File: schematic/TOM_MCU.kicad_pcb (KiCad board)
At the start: 4 copper layers, 236 parts, among them J1 22053041, J10 Conn_01x02, J11 Conn_01x02, J2 22053041, J3 USB4216-03-A, J4 USB4216-03-A, J5 E1E2-Emulator-Interface, J6 EMU CFG, J7 UPSEL_CFG, J8 Conn_01x02, J9 Conn_01x02, SW1 OP_CFG, U1 TVS2200DRV, U10 DS18B20+, U2 TVS2200DRV, U3 LDL1117S33R, U4 CY7C65213A-28PVXI, U5 TPS2116DRLR, U6 TXS0102DCUT, U7 TXS0102DCUT, U8 MIC5205-2.5YM5-TR, U9 R5F572NNHGFP-30, Y1 ECS-240-8-30B-CKM-TR

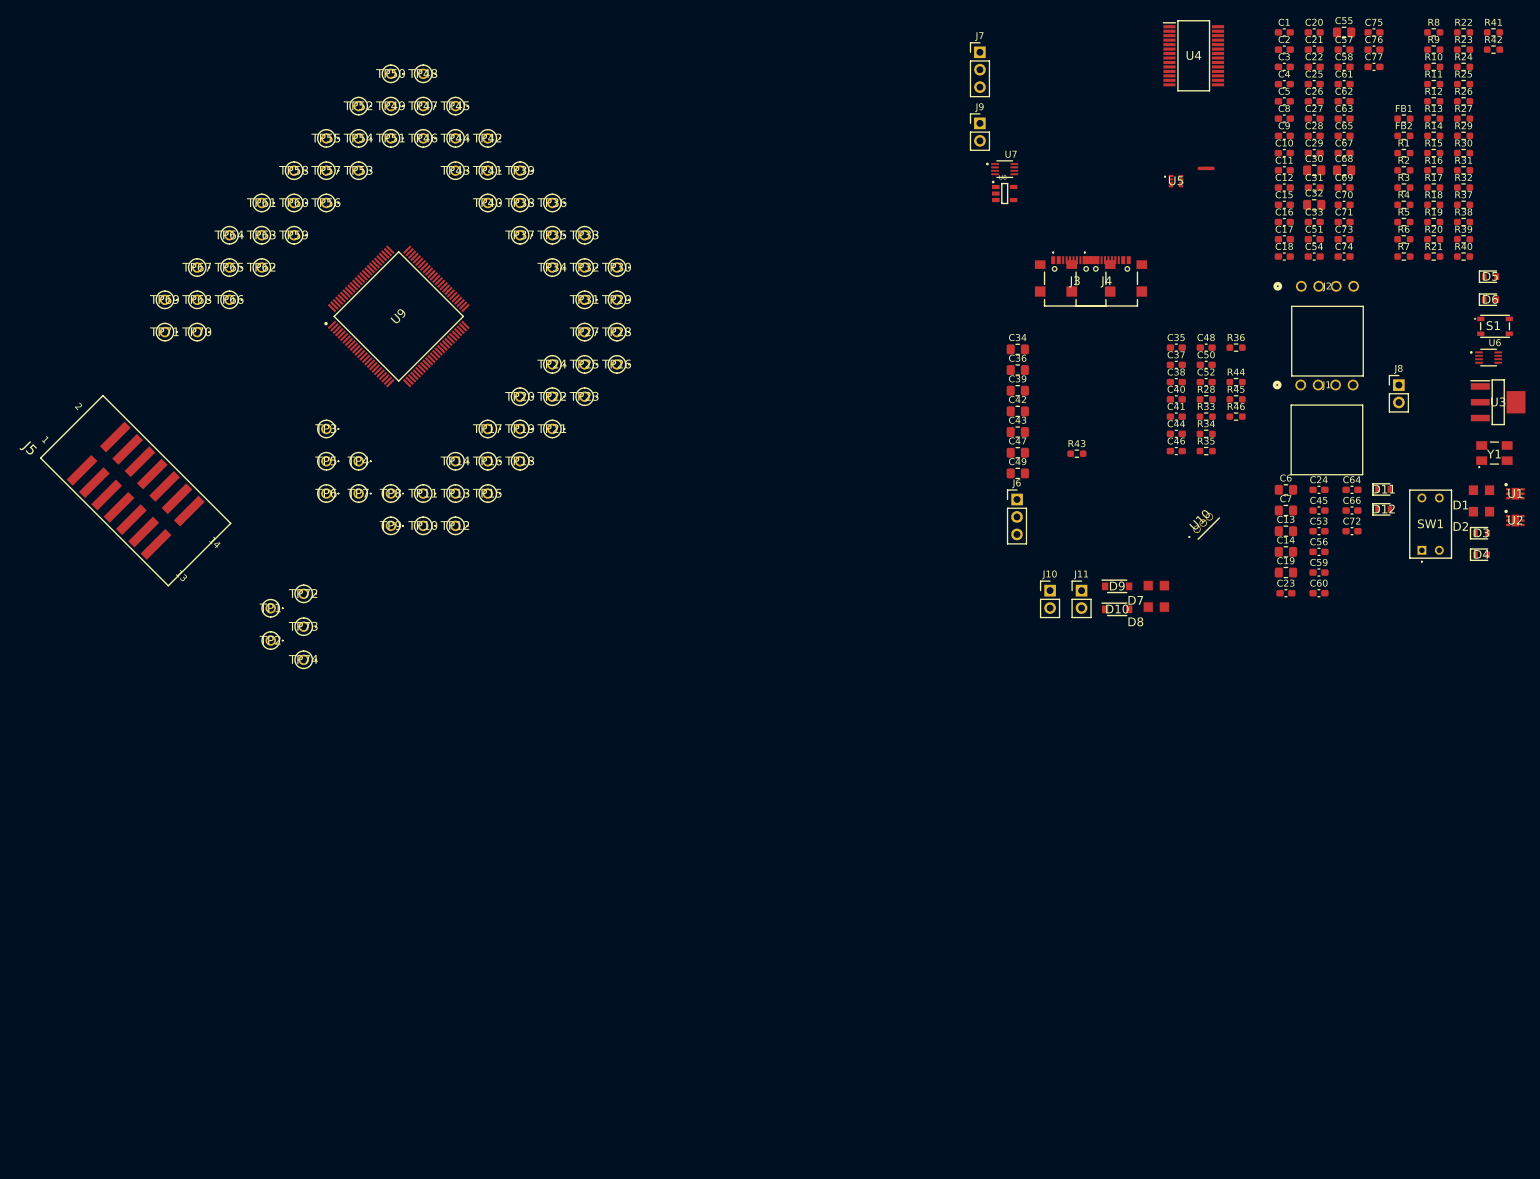
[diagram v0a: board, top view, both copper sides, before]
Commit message: TOM_MCU PCB
I think that we can remove Priority Switchover unless we wanted to add the 3v3 buck test pin into it. Or remove it and have BUS_3V3 be the board 3v3. Plus I left the other pins currently disconnected on the R5F5, but left the labels there currently, for if we wanted to add more test points.
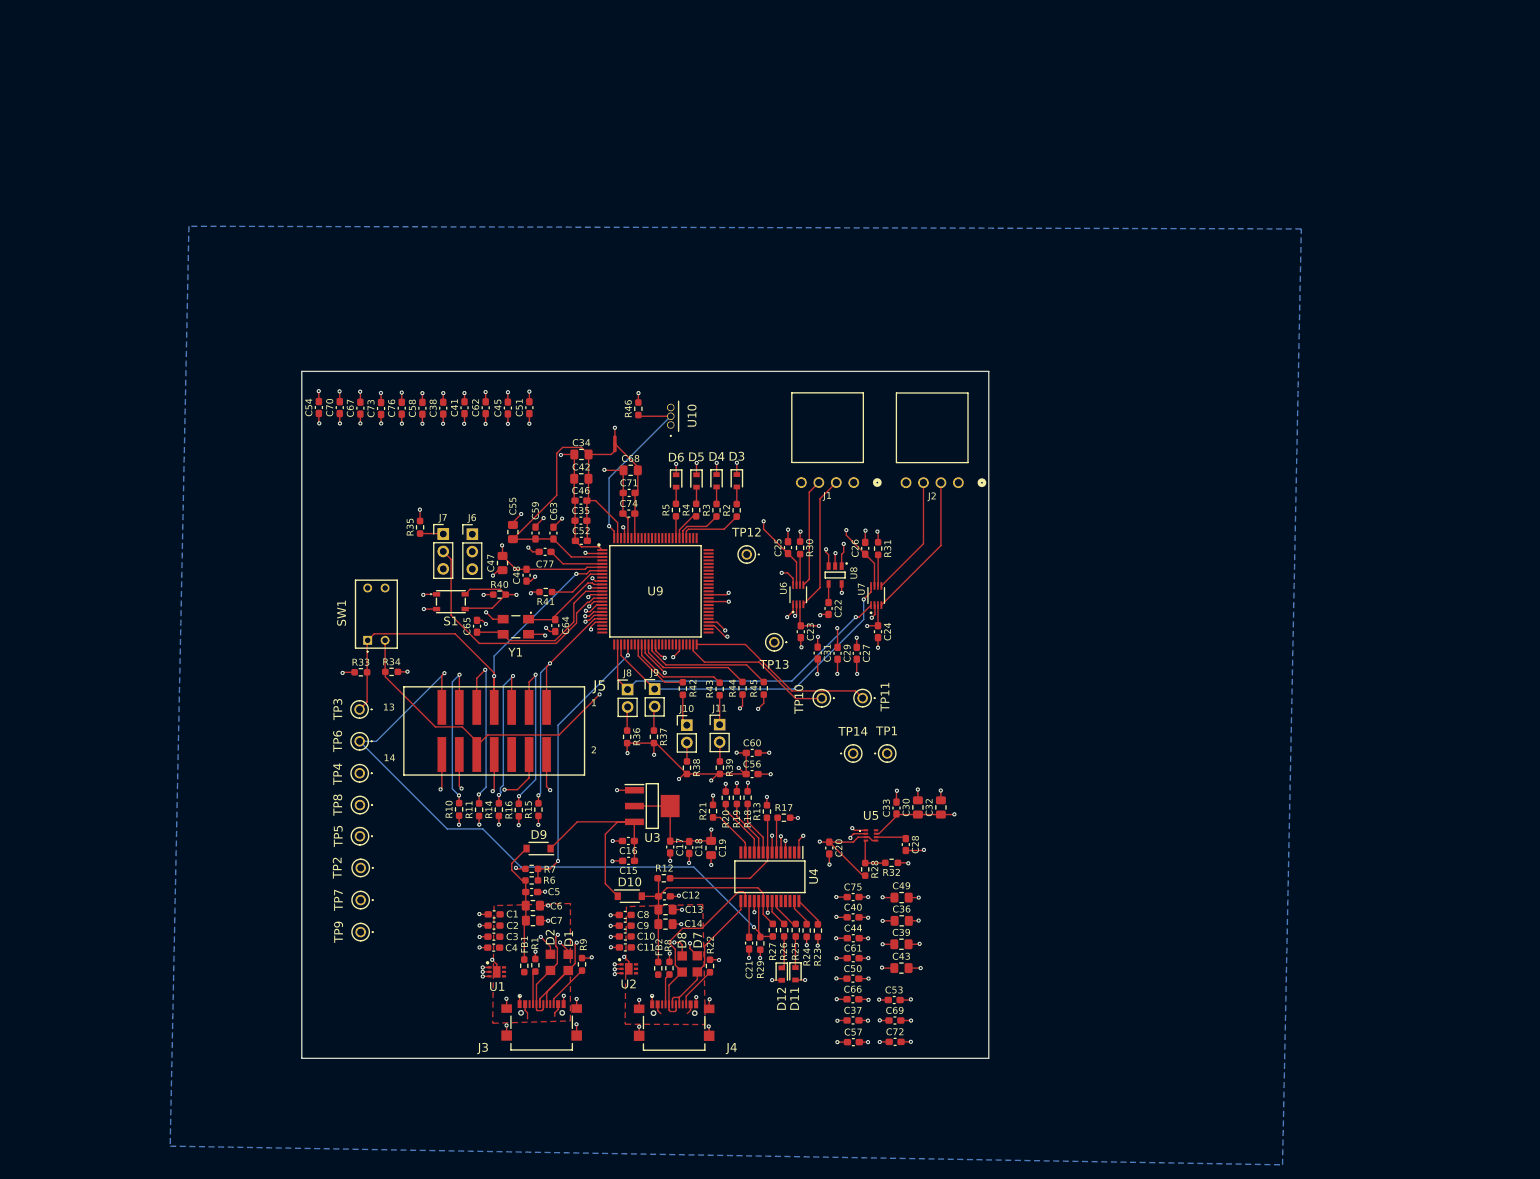
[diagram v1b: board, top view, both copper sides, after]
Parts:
- removed TP15, TP16, TP17, TP18, TP19, TP20, TP21, TP22, TP23, TP24, TP25, TP26, TP27, TP28, TP29, TP30, TP31, TP32, TP33, TP34, TP35, TP36, TP37, TP38, TP39, TP40, TP41, TP42, TP43, TP44, TP45, TP46, TP47, TP48, TP49, TP50, TP51, TP52, TP53, TP54, TP55, TP56, TP57, TP58, TP59, TP60, TP61, TP62, TP63, TP64, TP65, TP66, TP67, TP68, TP69, TP70, TP71, TP72, TP73, TP74: 3825, 3825:3825
- moved R9 181.9 mm to (297.8, 270.1), turned to -90 degrees
- moved R10 178.4 mm to (279.9, 247.6), turned to 90 degrees
- moved FB1 177.8 mm to (289.4, 270.3), turned to 90 degrees
- moved R8 175.9 mm to (310.5, 270.7), turned to -90 degrees
- moved R22 174.7 mm to (316.4, 270.4), turned to -90 degrees
- moved R11 174.6 mm to (282.8, 247.6), turned to 90 degrees
- moved R1 173.1 mm to (291.0, 270.3), turned to -90 degrees
- moved C1 172.4 mm to (285.0, 262.9)
- moved C2 171.7 mm to (285.0, 264.5)
- moved C3 171.1 mm to (285.0, 266.1)
- moved C4 170.4 mm to (285.0, 267.7)
- moved R14 167.8 mm to (285.7, 247.6), turned to 90 degrees
- moved U1 163.8 mm to (285.4, 271.2)
- moved FB2 162.7 mm to (308.9, 270.7), turned to 90 degrees
- moved R16 162.5 mm to (288.6, 247.7), turned to -90 degrees
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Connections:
- net Net-(J3-VBUS_1) renamed /USB0_VBUS
- net Net-(J4-VBUS_1) renamed /SCI_USBC_VBUS
- TP10 pad 1: /BMS_I2C_CLK -> /PMOD_JC_SDA
- TP11 pad 1: /BMS_I2C_DATA -> /PMOD_JC_SCL
- TP12 pad 1: /RSPIC_MOTOR0_nCS -> /BMS_SMBUS_DATA
- TP13 pad 1: /ENCODER0_PHASE_B -> /BMS_SMBUS_CLK
- TP14 pad 1: /ENCODER1_PHASE_A -> GND
- TP2 pad 1: /BOARD_3V3 -> /EMU_EMLE
- TP3 pad 1: /RSPIC_MOTOR2_nCS -> /DSW_MD_FINED
- TP6 pad 1: /ENCODER3_PHASE_A -> /DBG_RESETn
- TP7 pad 1: /ENCODER0_PHASE_A -> /EMU_TRSTn
- TP8 pad 1: /RSPIC_MOTOR1_nCS -> /EMU_TMS
- TP9 pad 1: /ENCODER1_PHASE_B -> /EMU_TCK
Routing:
- net GND: track 0.00 -> 210.7 mm, vias 0 -> 127
- net /BOARD_3V3: track 0.00 -> 206.7 mm, vias 0 -> 64
- net /DBG_RESETn: track 0.00 -> 158.9 mm, vias 0 -> 5
- net /EMU_EMLE: track 0.00 -> 95.8 mm, vias 0 -> 2
- net /EMU_TCK: track 0.00 -> 73.6 mm, vias 0 -> 2
- net /EMU_TRSTn: track 0.00 -> 73.3 mm, vias 0 -> 3
- net /DSW_MD_FINED: track 0.00 -> 65.1 mm, vias 0 -> 2
- net /EMU_TDO_TXD: track 0.00 -> 64.9 mm, vias 0 -> 3
- net /USB0_USBC_USBDP: track 0.00 -> 64.7 mm, vias 0 -> 2
- net /EMU_TDI_RXD: track 0.00 -> 64.5 mm, vias 0 -> 3
- net /EMU_TMS: track 0.00 -> 64.4 mm, vias 0 -> 3
- net /DSW_UB: track 0.00 -> 61.9 mm, vias 0 -> 2
- net /USB0_USBC_USBDN: track 0.00 -> 60.3 mm, vias 0 -> 2
- net AVSS0-1: track 0.00 -> 59.5 mm
- net /BUS_3V3: track 0.00 -> 50.5 mm, vias 0 -> 2
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- added copper zone on In2.Cu, net /BOARD_2V5
- added copper zone on In2.Cu, net /BOARD_3V3
- added copper zone on F.Cu, net /SCI_USBC_VBUS
- added copper zone on F.Cu, net /USB0_VBUS
- added copper zone on B.Cu, net GND
- added copper zone on In1.Cu, net GND
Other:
- board outline added: 100 x 100 mm

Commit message: Redo after Review #1
Double check USBC Data lines should be within spec.
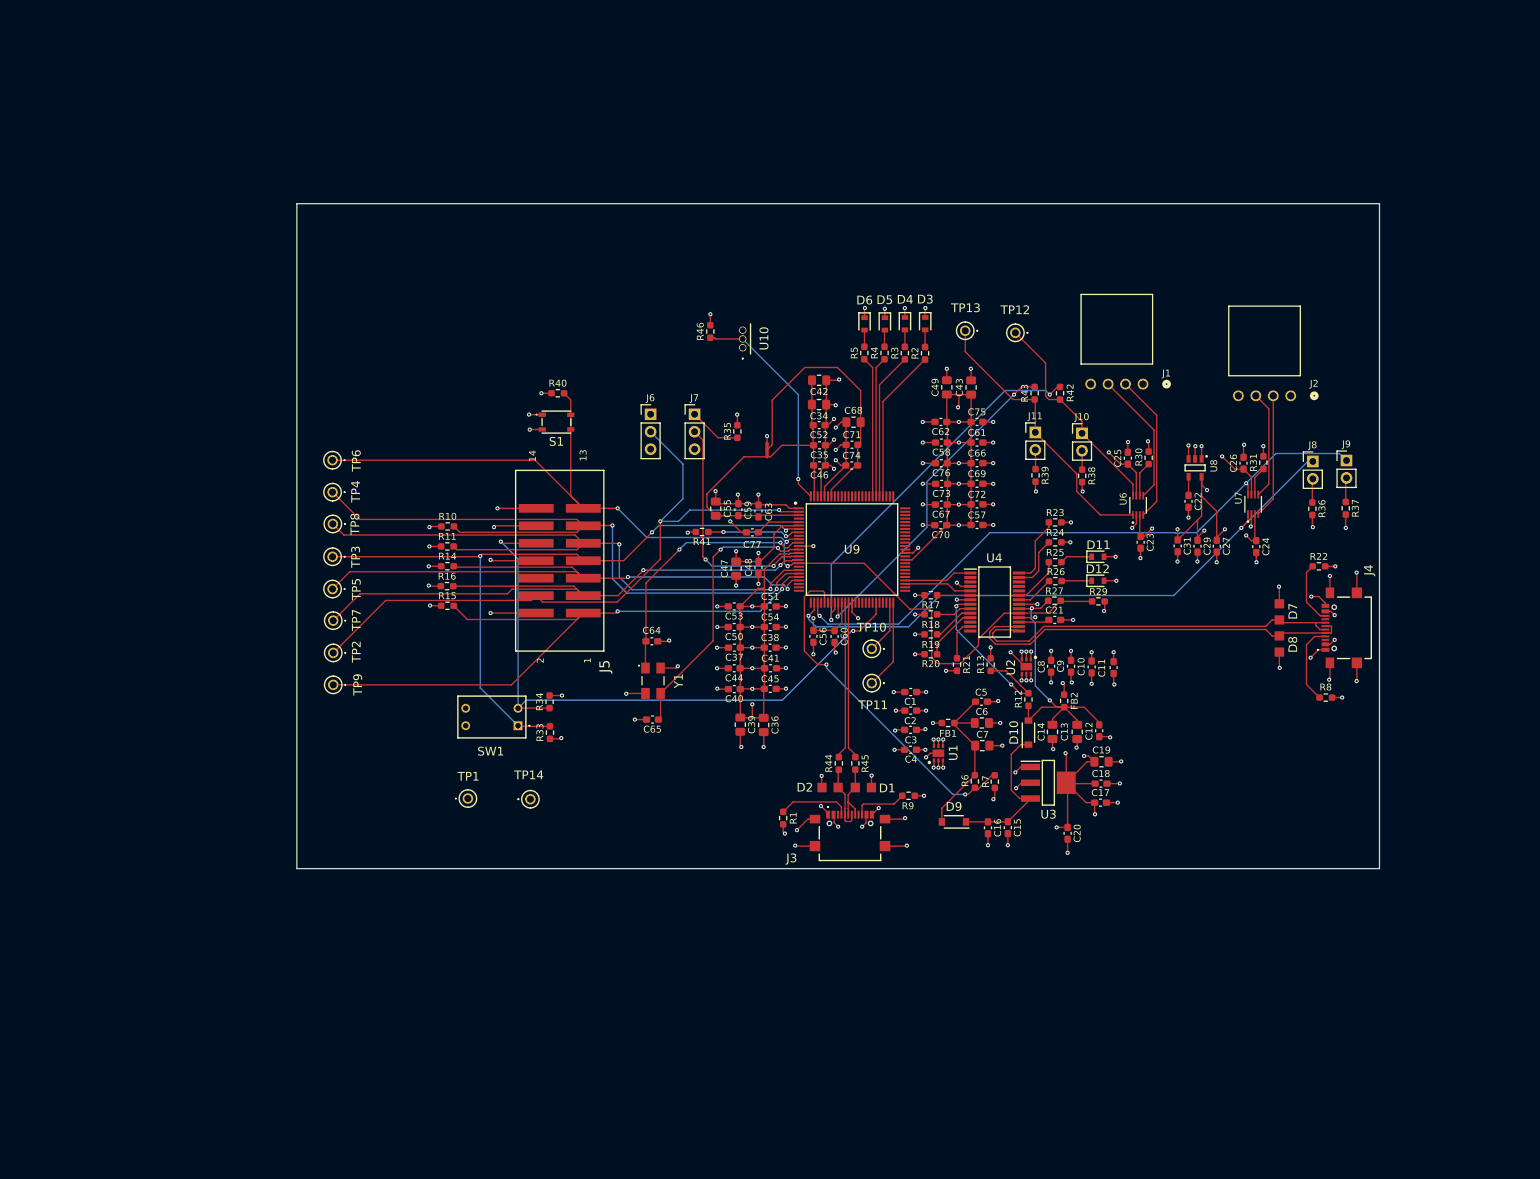
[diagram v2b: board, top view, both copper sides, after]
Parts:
- removed C28, C33: 1u, Capacitor_SMD:C_0603_1608Metric_Pad1.08x0.95mm_HandSolder
- removed C30, C32: 10u, Capacitor_SMD:C_0805_2012Metric_Pad1.18x1.45mm_HandSolder
- removed R28, R32: 10k, Resistor_SMD:R_0603_1608Metric_Pad0.98x0.95mm_HandSolder
- removed U5: TPS2116DRLR, TPS2116DRLR:TPS62932DRLR
- moved J4 114.1 mm to (409.4, 221.2), turned to 90 degrees
- moved J9 106.1 mm to (409.1, 196.8)
- moved R37 106.1 mm to (409.0, 203.7)
- moved R22 106.0 mm to (405.1, 212.2), turned to 180 degrees
- moved R36 105.1 mm to (404.1, 203.8)
- moved J8 105.1 mm to (404.2, 196.9)
- moved R8 103.3 mm to (406.1, 231.3), turned to 180 degrees
- moved D7 99.0 mm to (399.3, 218.8)
- moved D8 98.6 mm to (399.3, 223.5), turned to -90 degrees
- moved C70 89.1 mm to (350.0, 206.2), turned to 180 degrees
- moved C67 85.7 mm to (350.1, 203.2), turned to 180 degrees
- moved C43 85.1 mm to (354.5, 186.2), turned to 90 degrees
- moved C73 82.3 mm to (350.2, 200.2), turned to 180 degrees
- moved C11 81.9 mm to (375.2, 226.9), turned to -90 degrees
- moved C66 80.1 mm to (355.3, 197.2)
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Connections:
- net Net-(U9-USB0_DM) renamed /RX72N_USB0_DN
- net Net-(U9-USB0_DP) renamed /RX72N_USB0_DP
- C17 pad 1: /BUS_3V3 -> /BOARD_3V3
- C18 pad 1: /BUS_3V3 -> /BOARD_3V3
- C19 pad 1: /BUS_3V3 -> /BOARD_3V3
- C20 pad 1: /BUS_3V3 -> /BOARD_3V3
- U3 pad 2: /BUS_3V3 -> /BOARD_3V3
- U3 pad 4: /BUS_3V3 -> /BOARD_3V3
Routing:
- net /BOARD_3V3: track 206.7 -> 321.2 mm, vias 64 -> 56
- net /USB0_USBC_USBDP: track 64.7 -> 9.27 mm, vias 2 -> 0
- net /BUS_3V3: track 50.5 -> 0.00 mm, vias 2 -> 0
- net /USB0_USBC_USBDN: track 60.3 -> 10.2 mm, vias 2 -> 0
- net Net-(U9-P13/TXD2): track 9.76 -> 55.3 mm, vias 0 -> 2
- net /BMS_I2C_DATA: track 48.5 -> 91.8 mm, vias 1 -> 2
- net /BMS_I2C_CLK: track 47.7 -> 89.0 mm, vias 1 -> 2
- net /DSW_MD_FINED: track 65.1 -> 102.6 mm, vias 2 -> 3
- net /SCI_USBC_USBDP: track 20.9 -> 57.1 mm
- net /EMU_TDI_RXD: track 64.5 -> 99.8 mm, vias 3 -> 2
- net Net-(U9-P12/RXD2): track 14.6 -> 48.5 mm, vias 0 -> 2
- net /DSW_UB: track 61.9 -> 94.6 mm
- net /EMU_TMS: track 64.4 -> 95.7 mm, vias 3 -> 2
- net /RX72N_PIN_54: track 40.4 -> 9.93 mm, vias 2 -> 0
- net /SCI_USBC_USBDN: track 28.8 -> 59.0 mm
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- added copper zone on In2.Cu, net /SCI_USBC_VBUS
- added copper zone on In2.Cu, net /USB0_VBUS
- removed copper zone on F.Cu, net /SCI_USBC_VBUS
- removed copper zone on F.Cu, net /USB0_VBUS
- removed copper zone on B.Cu, net GND
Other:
- board size 100 x 100 mm -> 157.6 x 96.8 mm

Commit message: Fixed everything from last push
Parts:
- added TP15: 3825, 3825:3825, F.Cu at (409.0, 183.1)
- added TP16: 3825, 3825:3825, F.Cu at (409.0, 189.7)
- added TP17: 3825, 3825:3825, F.Cu at (360.5, 204.4)
- added TP18: 3825, 3825:3825, F.Cu at (360.5, 209.0)
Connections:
- U9 pad 100: /DS18B20_DQ -> unconnected-(U9-P05-Pad100)
- U9 pad 18: /RSPIC_MOTOR2_nCS -> unconnected-(U9-P32-Pad18)
- U9 pad 23: /ENCODER3_PHASE_A -> unconnected-(U9-P25-Pad23)
- U9 pad 24: /ENCODER0_PHASE_A -> unconnected-(U9-P24-Pad24)
- U9 pad 25: /RSPIC_MOTOR1_nCS -> unconnected-(U9-P23-Pad25)
- U9 pad 26: /ENCODER1_PHASE_B -> unconnected-(U9-P22-Pad26)
- U9 pad 29: /RSPIC_MOTOR0_nCS -> unconnected-(U9-P17-Pad29)
- U9 pad 31: /ENCODER0_PHASE_B -> unconnected-(U9-P15/RXD1-Pad31)
- U9 pad 32: /ENCODER1_PHASE_A -> unconnected-(U9-P14-Pad32)
- U9 pad 39: /PMOD_JB_GPIO1 -> unconnected-(U9-P55-Pad39)
- U9 pad 40: /PMOD_JB_GPIO2 -> unconnected-(U9-P54-Pad40)
- U9 pad 41: /PMOD_JA_SCK -> unconnected-(U9-P53-Pad41)
- U9 pad 42: /PMOD_JA_CS0 -> unconnected-(U9-P52-Pad42)
- U9 pad 43: /PMOD_JA_CIPO -> unconnected-(U9-P51-Pad43)
- U9 pad 44: /PMOD_JA_COPI -> unconnected-(U9-P50-Pad44)
- U9 pad 46: /PMOD_JB_GPIO0 -> unconnected-(U9-PC6-Pad46)
- U9 pad 47: /PMOD_JC_INT2 -> unconnected-(U9-PC5-Pad47)
- U9 pad 48: /PMOD_JC_INT1 -> unconnected-(U9-PC4-Pad48)
- U9 pad 51: /ENCODER2_PHASE_A -> unconnected-(U9-PC1-Pad51)
- U9 pad 52: /ENCODER2_PHASE_B -> unconnected-(U9-PC0-Pad52)
- U9 pad 55: /PMOD_JA_CS1 -> unconnected-(U9-PB5-Pad55)
- U9 pad 56: /PMOD_JA_DC -> unconnected-(U9-PB4-Pad56)
- U9 pad 57: /PMOD_JA_RST -> unconnected-(U9-PB3-Pad57)
- U9 pad 58: /PMOD_JA_GPIO -> unconnected-(U9-PB2-Pad58)
- U9 pad 59: /PMOD_JE_GPIO1 -> unconnected-(U9-PB1-Pad59)
- U9 pad 61: /PMOD_JE_GPIO2 -> unconnected-(U9-PB0-Pad61)
- U9 pad 63: /RPI5_RSPIA_CIPO -> unconnected-(U9-PA7-Pad63)
- U9 pad 64: /RPI5_RSPIA_COPI -> unconnected-(U9-PA6-Pad64)
- U9 pad 65: /RPI5_RSPIA_SCLK -> unconnected-(U9-PA5-Pad65)
- U9 pad 66: /RPI5_RSPIA_CS -> unconnected-(U9-PA4-Pad66)
- U9 pad 67: /ENCODER3_PHASE_B -> unconnected-(U9-PA3-Pad67)
- U9 pad 68: /PMOD_JB_GPIO3 -> unconnected-(U9-PA2-Pad68)
- U9 pad 69: /PMOD_JE_GPIO3 -> unconnected-(U9-PA1-Pad69)
- U9 pad 70: /RSPIC_MOTOR3_nCS -> unconnected-(U9-PA0-Pad70)
- U9 pad 71: /MOTOR3_PH -> unconnected-(U9-PE7-Pad71)
- U9 pad 72: /MOTOR3_EN -> unconnected-(U9-PE6-Pad72)
- U9 pad 73: /MOTOR0_PH -> unconnected-(U9-PE5-Pad73)
- U9 pad 74: /MOTOR1_PH -> unconnected-(U9-PE4-Pad74)
- U9 pad 75: /MOTOR2_PH -> unconnected-(U9-PE3-Pad75)
- U9 pad 76: /MOTOR0_EN -> unconnected-(U9-PE2-Pad76)
- U9 pad 77: /MOTOR1_EN -> unconnected-(U9-PE1-Pad77)
- U9 pad 78: /MOTOR2_EN -> unconnected-(U9-PE0-Pad78)
- U9 pad 79: /PMOD_JD_GPIO0 -> unconnected-(U9-PD7-Pad79)
- U9 pad 80: /PMOD_JD_GPIO1 -> unconnected-(U9-PD6-Pad80)
- U9 pad 81: /PMOD_JD_GPIO2 -> unconnected-(U9-PD5-Pad81)
- U9 pad 82: /PMOD_JD_GPIO3 -> unconnected-(U9-PD4-Pad82)
- U9 pad 83: /RSPIC_SCLK -> unconnected-(U9-PD3-Pad83)
- U9 pad 84: /RSPIC_CIPO -> unconnected-(U9-PD2-Pad84)
- U9 pad 85: /RSPIC_COPI -> unconnected-(U9-PD1-Pad85)
- U9 pad 86: /PMOD_JF_GPIO0 -> unconnected-(U9-PD0-Pad86)
- U9 pad 87: /MOTOR3_nFAULT -> unconnected-(U9-P47-Pad87)
- U9 pad 88: /MOTOR2_nFAULT -> unconnected-(U9-P46-Pad88)
- U9 pad 89: /MOTOR1_nFAULT -> unconnected-(U9-P45-Pad89)
- U9 pad 90: /MOTOR0_nFAULT -> unconnected-(U9-P44-Pad90)
- U9 pad 91: /MOTOR3_IPROPI -> unconnected-(U9-P43-Pad91)
- U9 pad 92: /MOTOR2_IPROPI -> unconnected-(U9-P42-Pad92)
- U9 pad 93: /MOTOR1_IPROPI -> unconnected-(U9-P41-Pad93)
- U9 pad 95: /MOTOR0_IPROPI -> unconnected-(U9-P40-Pad95)
- U9 pad 98: /PMOD_JF_GPIO1 -> unconnected-(U9-P07-Pad98)
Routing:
- net /BMS_I2C_CLK: track 89.0 -> 104.8 mm
- net /RX72N_PIN_54: track 9.93 -> 22.0 mm
- net /RX72N_PIN_53: track 9.90 -> 20.0 mm
- net /BMS_I2C_DATA: track 91.8 -> 98.9 mm
- net /SCI_USBC_USBDN: track 59.0 -> 56.0 mm
- net /SCI_USBC_USBDP: track 57.1 -> 55.6 mm
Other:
- board size 157.6 x 96.8 mm -> 156.3 x 96.8 mm
